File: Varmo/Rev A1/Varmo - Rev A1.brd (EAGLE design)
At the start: 162.6 x 114.3 mm, 67 parts, among them U1 ATMEGA328, U2 SN74LVC2G17DBVR, U3 SN74LVC2G17DBVR, U4 90814-0210, U5 90814-0210, X1 NC5MAH, X2 SMKDSP_1,5/3, X3 SMKDSP_1,5/2, X4 SMKDSP_1,5/2, Y1 8MHz

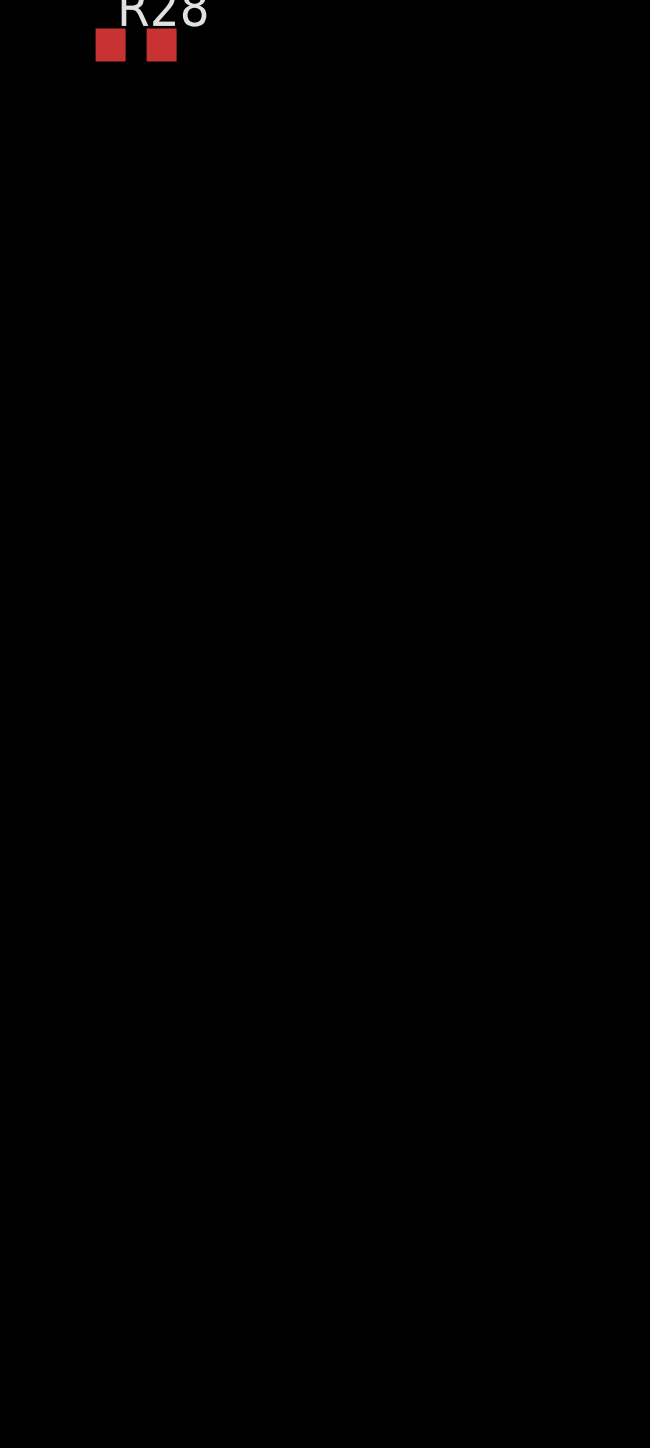
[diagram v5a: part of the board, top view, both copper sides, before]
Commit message: Update International_Rectfier_By_element14_Batch_1.lbr, Update Varmo Rev A1 schematic
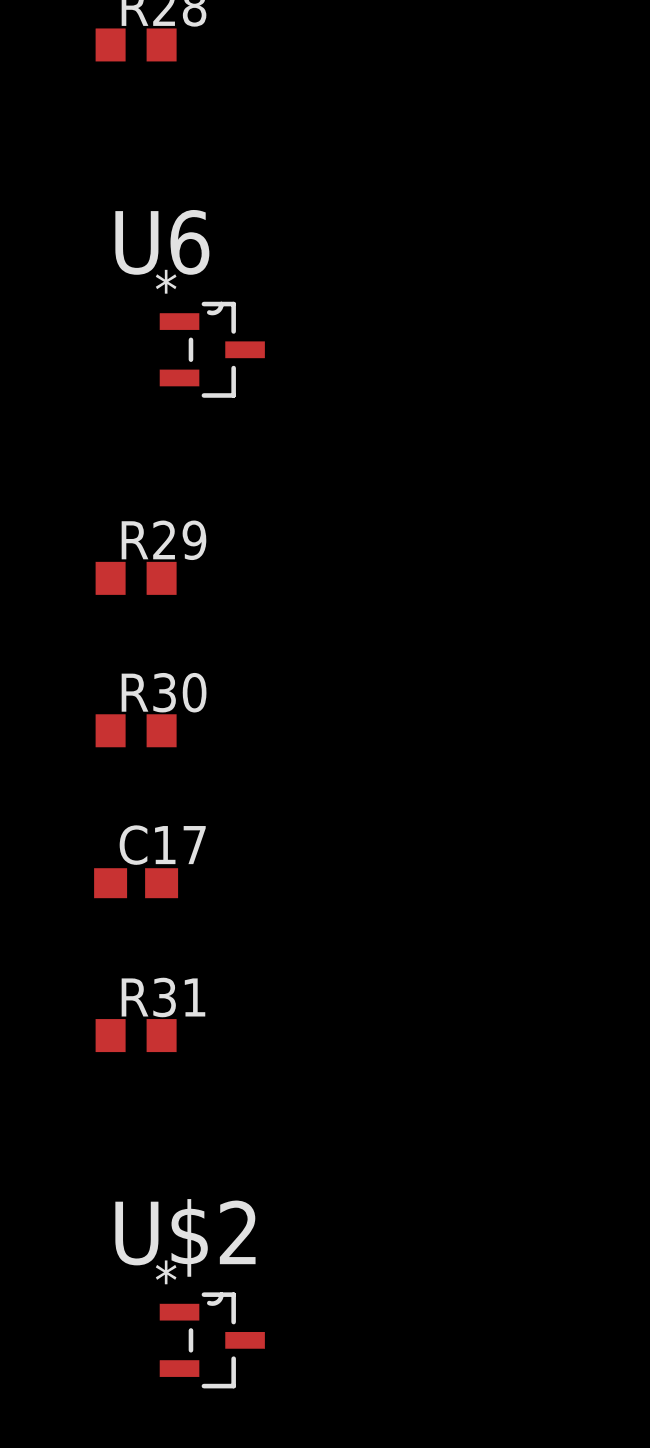
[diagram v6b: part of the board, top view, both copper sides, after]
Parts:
- added C17: 0.1uF, rcl:C0603
- added R29, R30, R31: 330, rcl:R0603
- added U$2: IRLML5103TRPBF, International_Rectifier_By_element14_Batch_1:SOT95P240X112-3N
- added U6: IRLML6344TRPBF, International_Rectifier_By_element14_Batch_1:SOT95P240X112-3N
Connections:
- removed net CONSTRASTE: U1.13
- new net CONTRASTE_PWM1: R31.2, U1.13
- new net CONTRASTE_PWM2: R29.2, U1.14
- new net N$17: R29.1, U6.1
- new net N$22: R30.2, U$2.3, U6.3
- new net N$24: R31.1, U$2.1
- net +5V/1: now also U$2.2
- net CONTRASTE: now also C17.1, R30.1
- net GND1: now also C17.2
- net VEE: now also U6.2
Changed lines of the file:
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@@
 <element name="R27" library="rcl" package="R0603" value="1.5k" x="-185.42" y="-403.86"/>
 <element name="R28" library="rcl" package="R0603" value="1.5k" x="-185.42" y="-408.94"/>
+<element name="U6" library="International_Rectifier_By_element14_Batch_1" package="SOT95P240X112-3N" value="IRLML6344TRPBF" x="-182.88" y="-419.1">
+<attribute name="SUPPLIER" value="INTERNATIONAL RECTIFIER" x="-182.88" y="-419.1" size="1.778" layer="27" display="off"/>
+<attribute name="OC_NEWARK" value="25T5501" x="-182.88" y="-419.1" size="1.778" layer="27" display="off"/>
+<attribute name="PACKAGE" value="SOT-23-3" x="-182.88" y="-419.1" size="1.778" layer="27" display="off"/>
+<attribute name="MPN" value="IRLML6344TRPBF" x="-182.88" y="-419.1" size="1.778" layer="27" display="off"/>
+<attribute name="OC_FARNELL" value="1857299" x="-182.88" y="-419.1" size="1.778" layer="27" display="off"/>
+</element>
+<element name="R29" library="rcl" package="R0603" value="330" x="-185.42" y="-426.72"/>
+<element name="R30" library="rcl" package="R0603" value="330" x="-185.42" y="-431.8"/>
+<element name="C17" library="rcl" package="C0603" value="0.1uF" x="-185.42" y="-436.88"/>
+<element name="R31" library="rcl" package="R0603" value="330" x="-185.42" y="-441.96"/>
+<element name="U$2" library="International_Rectifier_By_element14_Batch_1" package="SOT95P240X112-3N" value="IRLML5103TRPBF" x="-182.88" y="-452.12"/>
 </elements>
 <signals>
@@
 <contactref element="U$1" pad="D"/>
 <contactref element="U$1" pad="C"/>
+<contactref element="C17" pad="2"/>
 <wire x1="-97.37" y1="-143.51" x2="-97.37" y2="-148.59" width="0" layer="19" extent="1-1"/>
 <wire x1="-95.67" y1="-132.08" x2="-97.37" y2="-143.51" width="0" layer="19" extent="1-1"/>
@@
 <wire x1="-180.3" y1="-346.06" x2="-126.15" y2="-304.8" width="0" layer="19" extent="1-1"/>
 <wire x1="-175.3" y1="-360.56" x2="-180.3" y2="-346.06" width="0" layer="19" extent="1-1"/>
+<wire x1="-184.57" y1="-436.88" x2="-175.3" y2="-360.56" width="0" layer="19" extent="1-1"/>
 <wire x1="97.79" y1="6.35" x2="-95.67" y2="-121.92" width="0" layer="19" extent="1-1"/>
 <wire x1="125.73" y1="6.35" x2="97.79" y2="6.35" width="0" layer="19" extent="1-1"/>
@@
 <contactref element="C15" pad="1"/>
 <contactref element="C16" pad="1"/>
+<contactref element="U$2" pad="2"/>
 <wire x1="-95.67" y1="-153.67" x2="-95.67" y2="-158.75" width="0" layer="19" extent="1-1"/>
 <wire x1="-95.67" y1="-127" x2="-95.67" y2="-153.67" width="0" layer="19" extent="1-1"/>
@@
 <wire x1="-127.85" y1="-299.72" x2="-123.1646" y2="-292.1" width="0" layer="19" extent="1-1"/>
 <wire x1="-127.85" y1="-304.8" x2="-127.85" y2="-299.72" width="0" layer="19" extent="1-1"/>
+<wire x1="-183.9722" y1="-453.0598" x2="-127.85" y2="-304.8" width="0" layer="19" extent="1-1"/>
 <wire x1="82.38" y1="17.65" x2="-95.67" y2="-127" width="0" layer="19" extent="1-1"/>
 <wire x1="100.33" y1="6.35" x2="82.38" y2="17.65" width="0" layer="19" extent="1-1"/>
@@
 <wire x1="88.82614375" y1="55.526796875" x2="94.3311125" y2="48.890459375" width="0" layer="19" extent="1-1"/>
 <wire x1="89.957515625" y1="56.65816875" x2="88.82614375" y2="55.526796875" width="0" layer="19" extent="1-1"/>
-<wire x1="87.63" y1="67.73" x2="88.82614375" y2="55.526796875" width="0" layer="19" extent="1-1"/>
+<wire x1="87.63" y1="67.73" x2="89.957515625" y2="56.65816875" width="0" layer="19" extent="1-1"/>
 <wire x1="85.09" y1="67.73" x2="87.63" y2="67.73" width="0" layer="19" extent="1-1"/>
 <wire x1="82.55" y1="67.73" x2="85.09" y2="67.73" width="0" layer="19" extent="1-1"/>
@@
 <wire x1="99.185" y1="82.55" x2="93.13" y2="81.28" width="0" layer="19" extent="1-1"/>
 <wire x1="113.03" y1="53.34" x2="94.3311125" y2="48.890459375" width="0" layer="19" extent="1-1"/>
-<wire x1="158.75" y1="71.43" x2="99.185" y2="82.55" width="0" layer="19" extent="1-1"/>
-<wire x1="158.33" y1="67.31" x2="158.75" y2="71.43" width="0" layer="19" extent="1-1"/>
+<wire x1="158.33" y1="67.31" x2="113.03" y2="53.34" width="0" layer="19" extent="1-1"/>
+<wire x1="158.75" y1="71.43" x2="158.33" y2="67.31" width="0" layer="19" extent="1-1"/>
 </signal>
 <signal name="ESW3_RX_ISO">
@@
 <contactref element="R6" pad="3"/>
 <contactref element="JP2" pad="15"/>
+<contactref element="U6" pad="2"/>
 <wire x1="80.18" y1="17.65" x2="133.35" y2="6.35" width="0" layer="19" extent="1-1"/>
+<wire x1="-183.9722" y1="-420.0398" x2="80.18" y2="17.65" width="0" layer="19" extent="1-1"/>
 </signal>
 <signal name="ENCODER_E">
@@
 <signal name="CONTRASTE">
 <contactref element="R26" pad="2"/>
-</signal>
-<signal name="CONSTRASTE">
-<contactref element="U1" pad="13"/>
+<contactref element="R30" pad="1"/>
+<contactref element="C17" pad="1"/>
+<wire x1="-186.27" y1="-431.8" x2="-186.27" y2="-436.88" width="0" layer="19" extent="1-1"/>
+<wire x1="-184.57" y1="-370.84" x2="-186.27" y2="-431.8" width="0" layer="19" extent="1-1"/>
 </signal>
 <signal name="N$15">
@@
 <wire x1="-184.57" y1="-403.86" x2="96.593853125" y2="51.1532" width="0" layer="19" extent="1-1"/>
 </signal>
+<signal name="N$17">
+<contactref element="R29" pad="1"/>
+<contactref element="U6" pad="1"/>
+<wire x1="-183.9722" y1="-418.1602" x2="-186.27" y2="-426.72" width="0" layer="19" extent="1-1"/>
+</signal>
+<signal name="N$22">
+<contactref element="U6" pad="3"/>
+<contactref element="R30" pad="2"/>
+<contactref element="U$2" pad="3"/>
+<wire x1="-184.57" y1="-431.8" x2="-181.7878" y2="-452.12" width="0" layer="19" extent="1-1"/>
+<wire x1="-181.7878" y1="-419.1" x2="-184.57" y2="-431.8" width="0" layer="19" extent="1-1"/>
+</signal>
+<signal name="N$24">
+<contactref element="R31" pad="1"/>
+<contactref element="U$2" pad="1"/>
+<wire x1="-186.27" y1="-441.96" x2="-183.9722" y2="-451.1802" width="0" layer="19" extent="1-1"/>
+</signal>
+<signal name="CONTRASTE_PWM1">
+<contactref element="R31" pad="2"/>
+<contactref element="U1" pad="13"/>
+<wire x1="-184.57" y1="-441.96" x2="89.957515625" y2="50.021828125" width="0" layer="19" extent="1-1"/>
+</signal>
+<signal name="CONTRASTE_PWM2">
+<contactref element="R29" pad="2"/>
+<contactref element="U1" pad="14"/>
+<wire x1="-184.57" y1="-426.72" x2="90.5232" y2="49.45614375" width="0" layer="19" extent="1-1"/>
+</signal>
 </signals>

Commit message: Update board of Varmo Rev 1, Update dc-dc-converter library
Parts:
- removed U$2: IRLML5103TRPBF, International_Rectifier_By_element14_Batch_1:SOT95P240X112-3N
- removed U6: IRLML6344TRPBF, International_Rectifier_By_element14_Batch_1:SOT95P240X112-3N
- removed X1: NC5MAH, con-neutrik_ag:NC5MAH
- added C18: 10pF, rcl:C0603
- added JP10, JP3, JP4, JP5, JP6, JP7, JP8, JP9: FIDUCIAL1X2, SparkFun:FIDUCIAL-1X2
- added MP1, MP2, MP3, MP4, MP5, MP6: MOUNT-PAD3,0, holes:P3,0
- added SJ1, SJ2, SJ3, SJ4, SJ5, SJ6, SJ7: (no value), jumper:SJ
- added T1: IRLML5103TRPBF, International_Rectifier_By_element14_Batch_1:SOT95P240X112-3N
- added T2: IRLML6344TRPBF, International_Rectifier_By_element14_Batch_1:SOT95P240X112-3N
- added X5: NC5MAV-SW, con-neutrik_ag:NC5MAV-SW
- R30: value 330 -> 10K
- moved C17 555.9 mm to (45.0, 69.0), flipped to the bottom, turned to 180 degrees
- moved R31 554.5 mm to (37.0, 66.0), flipped to the bottom
- moved R30 548.3 mm to (44.5, 66.0), flipped to the bottom, turned to 270 degrees
- moved R29 544.2 mm to (37.0, 70.0), flipped to the bottom
- moved R27 512.5 mm to (89.0, 29.0), turned to 180 degrees
- moved R26 503.8 mm to (41.5, 79.0), flipped to the bottom, turned to 270 degrees
- moved R28 502.5 mm to (89.0, 12.0), turned to 180 degrees
- moved R25 497.3 mm to (37.0, 79.0), flipped to the bottom, turned to 270 degrees
- moved LED5 495.0 mm to (97.0, 29.0)
- moved LED6 491.4 mm to (97.0, 12.0)
- moved R24 473.2 mm to (-26.7, 105.4)
- moved R23 470.2 mm to (-21.6, 105.4)
- moved R22 467.2 mm to (-16.5, 105.4)
- moved U$1 445.8 mm to (60.0, 24.0)
- moved R21 434.9 mm to (-95.2, 100.3)
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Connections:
- new net 1: MP1.1, MP2.1, MP3.1, MP4.1, MP5.1, MP6.1, SJ1.1, SJ2.1, SJ3.1, SJ4.1, SJ6.1, SJ7.1
- new net N$23: SJ5.2, X5.G
- net +5V/1: now also T1.2; no longer U$2.2
- net 5V: now also X5.5; no longer X1.5
- net CONTRASTE: now also C18.1
- net CONTRASTE_PWM1: now also U1.9; no longer U1.13
- net CONTRASTE_PWM2: now also U1.10; no longer U1.14
- net DIRECTION_1: now also U1.12; no longer U1.25
- net DIRECTION_2: now also U1.13; no longer U1.26
- net ESW3_CMD: now also U1.11; no longer U1.9
- net GND: now also X5.1; no longer LED5.K, LED6.K, X1.1
- net GND1: now also C18.2, LED5.K, LED6.K
- net GND2: now also SJ1.2, SJ2.2, SJ3.2, SJ4.2, SJ5.1, SJ6.2, SJ7.2; no longer X1.G
- net N$17: now also T2.1; no longer U6.1
- net N$22: now also T1.3, T2.3; no longer U$2.3, U6.3
- net N$24: now also T1.1; no longer U$2.1
- net PUSH_BUTTON_2: now also U1.14; no longer U1.24
- net RX: now also X5.2; no longer X1.2
- net TOR: now also X5.4; no longer X1.4
- net TX: now also X5.3; no longer X1.3
- net VEE: now also T2.2; no longer U6.2
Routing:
- net 1: track 0.00 -> 233.1 mm
- net GND2: track 0.00 -> 199.5 mm
- net ESW3_ISO: track 0.00 -> 112.5 mm, vias 0 -> 5
- net RESET: track 0.00 -> 75.5 mm, vias 0 -> 2
- net GND1: track 0.00 -> 69.6 mm, vias 0 -> 8
- net ESW3_TX_ISO: track 0.00 -> 67.7 mm
- net SCK: track 0.00 -> 52.9 mm, vias 0 -> 2
- net ENCODER_E: track 0.00 -> 52.2 mm, vias 0 -> 2
- net MISO: track 0.00 -> 51.0 mm, vias 0 -> 2
- net MOSI: track 0.00 -> 50.8 mm, vias 0 -> 2
- net ESW3_RX_ISO: track 0.00 -> 49.5 mm
- net BUTTON_1: track 0.00 -> 48.8 mm, vias 0 -> 3
- net ENCODER_A: track 0.00 -> 47.6 mm, vias 0 -> 2
- net LED_1: track 0.00 -> 46.5 mm
- net ENCODER_B: track 0.00 -> 46.4 mm, vias 0 -> 2
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- added copper zone on layer 1, net +5V/1
- added copper zone on layer 16, net GND1
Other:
- board size 162.6 x 114.3 mm -> 118 x 135 mm

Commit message: Removed eagle.epf files, update Varmo Rev A1 schematic and board, add P2.5mm to holes.lbr, update midas.lbr
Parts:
- removed JP2: (no value), pinhead:1X16
- removed LED6: RED, led:LED10MM
- removed MP1, MP2, MP3, MP4: MOUNT-PAD3,0, holes:P3,0
- removed R22, R23, R24: 1.5k, rcl:R0603
- removed SJ1, SJ2, SJ3, SJ4: (no value), jumper:SJ
- added J1, J2: 22-05-7028-02, con-molex:7395-02
- added LCD1: MC21605G-VNMLWI, midas:MC21605G
- added R32, R33, R34, R35: 1.5k, rcl:R0603
- added U$2, U$3, U$4, U$5: (no value), mentor:1275.100
- LED5: value GRN -> Green; device led:LED10MM -> led:CHIP-LED0603
- MP5, MP6: value MOUNT-PAD3,0 -> MOUNT-PAD2.5; device holes:P3,0 -> holes:P2.5
- moved LED2 200.3 mm to (120.8, 9.00)
- moved LED4 195.9 mm to (105.8, 9.00)
- moved LED1 190.1 mm to (120.8, 24.0)
- moved LED3 185.6 mm to (105.8, 24.0)
- moved SJ5 175.5 mm to (106.8, 46.7), flipped to the bottom, turned to 180 degrees
- moved U4 173.6 mm to (116.4, 37.4), flipped to the bottom
- moved U5 159.6 mm to (84.6, 4.57), flipped to the bottom, turned to 90 degrees
- moved X5 140.9 mm to (110.6, 54.8)
- moved C3 132.8 mm to (16.5, 15.2), turned to 90 degrees
- moved R21 127.7 mm to (13.8, 33.8), turned to 180 degrees
- moved C2 125.7 mm to (14.2, 15.2), turned to 90 degrees
- moved OK3 113.1 mm to (22.2, 22.2), turned to 0 degrees
- moved C1 104.7 mm to (7.75, 33.8)
- moved C8 104.2 mm to (24.5, 14.5), flipped to the top, turned to 180 degrees
- moved OK1 91.4 mm to (38.0, 22.2), turned to 180 degrees
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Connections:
- removed net 5V: R24.2, U4.8, X5.5
- removed net GND2: SJ1.2, SJ2.2, SJ3.2, SJ4.2, SJ5.1, SJ6.2, SJ7.2
- removed net N$18: LED1.A, R21.1
- removed net N$19: LED2.A, R22.1
- removed net N$20: LED3.A, R23.1
- removed net N$21: LED4.A, R24.1
- removed net SA0: JP2.7, R2.2
- removed net SA1: JP2.8, R3.2
- new net N$29: LCD1.8, R2.2
- new net N$30: LCD1.7, R3.2
- new net N$31: LED1.A, R32.1
- new net N$32: LED2.A, R33.1
- new net N$33: LED3.A, R34.1
- new net N$34: LED4.A, R35.1
- new net N$35: LED5.A, R21.1
- net +5V: now also R35.2, U4.8, X5.5
- net +5V/1: now also LCD1.2, R21.2; no longer JP2.2
- net 1: no longer MP1.1, MP2.1, MP3.1, MP4.1, SJ1.1, SJ2.1, SJ3.1, SJ4.1
- net BUTTON_1: now also U1.19; no longer U1.23
- net CONTRASTE_PWM1: now also U1.10; no longer U1.9
- net CONTRASTE_PWM2: now also U1.9; no longer U1.10
- net ESW3: now also R34.2
- net ESW3_RX: now also R33.2
- net ESW3_TX: now also R32.2
- net GND: now also SJ5.1
- net GND1: now also J1.2, J2.2, LCD1.1, LCD1.12, LCD1.16, LED5.C, SJ6.2, SJ7.2; no longer JP2.1, JP2.12, JP2.16, LED5.K, LED6.K
- net LED_1: now also U1.23; no longer U1.19
- net LED_2: now also U1.24; no longer U1.22
- net N$15: now also J2.1; no longer LED5.A
- net N$16: now also J1.1; no longer LED6.A
- net RX: no longer R21.2
- net SCL: now also LCD1.14; no longer JP2.14
- net SDA: now also LCD1.13; no longer JP2.13
- net TOR: no longer R23.2
- net TX: no longer R22.2
- net VEE: now also LCD1.15; no longer JP2.15
- net VO: now also LCD1.3; no longer JP2.3
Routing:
- net 1: track 233.1 -> 10.5 mm
- net GND2: track 199.5 -> 0.00 mm
- net SCL: track 35.4 -> 148.5 mm
- net ESW3_TX: track 0.00 -> 112.6 mm, vias 0 -> 2
- net SDA: track 41.0 -> 149.5 mm, vias 1 -> 2
- net ESW3: track 0.00 -> 92.4 mm, vias 0 -> 2
- net ESW3_RX: track 0.00 -> 92.2 mm, vias 0 -> 2
- net CONTRASTE_PWM2: track 32.8 -> 94.5 mm
- net CONTRASTE_PWM1: track 24.5 -> 85.7 mm
- net LED_1: track 46.5 -> 103.1 mm, vias 0 -> 2
- net LED_2: track 36.1 -> 90.3 mm, vias 0 -> 2
- net VEE: track 3.97 -> 49.4 mm, vias 0 -> 1
- net RX: track 0.00 -> 31.5 mm, vias 0 -> 2
- net RESET: track 75.5 -> 48.1 mm, vias 2 -> 1
- net TOR: track 0.00 -> 25.1 mm
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- added copper zone on layer 1, net +5V
- added copper zone on layer 16, net GND
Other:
- board size 118 x 135 mm -> 126 x 120.5 mm
- board text added: "+5V"
- board text added: "BUTTON1"
- board text added: "BUTTON2"
- board text added: "DIR1"
- board text added: "DIR2"
- board text added: "ESW3"
- board text added: "GND"
- board text added: "ON"
- board text added: "RX"
- board text added: "TX"
